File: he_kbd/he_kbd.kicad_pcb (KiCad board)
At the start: 2 copper layers, 162.2 x 126.5 mm, 165 parts, among them U1 CD74HC4067M, U2 CD74HC4067M, U3 CD74HC4067M

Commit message: continue
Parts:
- U1, U2, U3: footprint Package_SO:SOIC-24W_7.5x15.4mm_P1.27mm -> Package_SO:SSOP-24_3.9x8.7mm_P0.635mm
- moved U3 2.47 mm to (78.8, 54.2)
- moved U1 2.37 mm to (101.4, 115.9)
- moved U2 2.19 mm to (81.2, 93.4)
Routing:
- net Net-(HE_9-OUT): track 59.5 -> 125.4 mm, vias 2 -> 1
- net Net-(HE_10-OUT): track 44.2 -> 30.3 mm, vias 2 -> 1
- net Net-(HE_3-OUT): track 27.9 -> 20.4 mm
- net Net-(HE_8-OUT): track 75.3 -> 79.4 mm
- net Net-(HE_11-OUT): track 27.4 -> 31.6 mm
- net /MTP_EN_0: track 3.88 -> 0.00 mm, vias 1 -> 0
- net /MTP_BIN_2: track 3.42 -> 0.00 mm, vias 1 -> 0
- net Net-(HE_2-OUT): track 46.5 -> 43.4 mm
- net Net-(HE_1-OUT): track 62.6 -> 65.7 mm
- net Net-(HE_6-OUT): track 62.3 -> 59.2 mm
- net /MTP_BIN_3: track 2.21 -> 0.00 mm, vias 1 -> 0
- net Net-(HE_16-OUT): track 1.84 -> 0.00 mm, vias 1 -> 0
- net Net-(HE_15-OUT): track 1.83 -> 0.00 mm, vias 1 -> 0
- net Net-(HE_14-OUT): track 1.82 -> 0.00 mm, vias 1 -> 0
- net Net-(HE_13-OUT): track 1.81 -> 0.00 mm, vias 1 -> 0
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
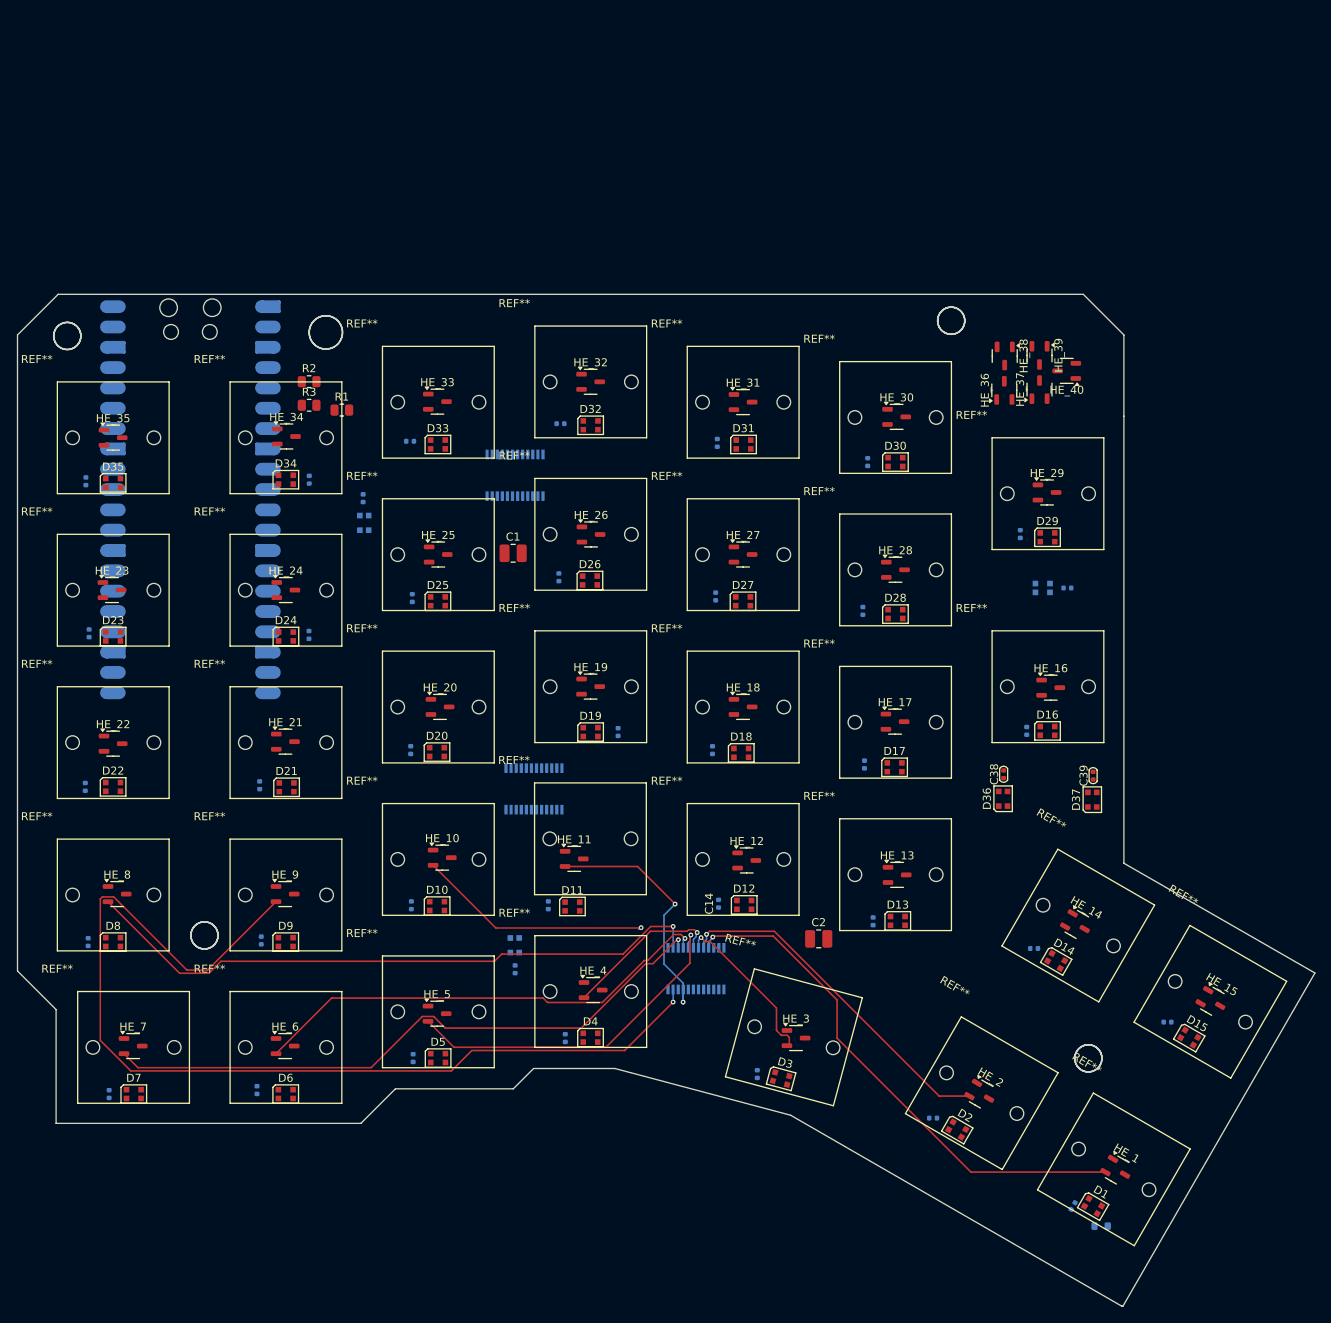
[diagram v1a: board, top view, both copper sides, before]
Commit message: fixed up the net classes
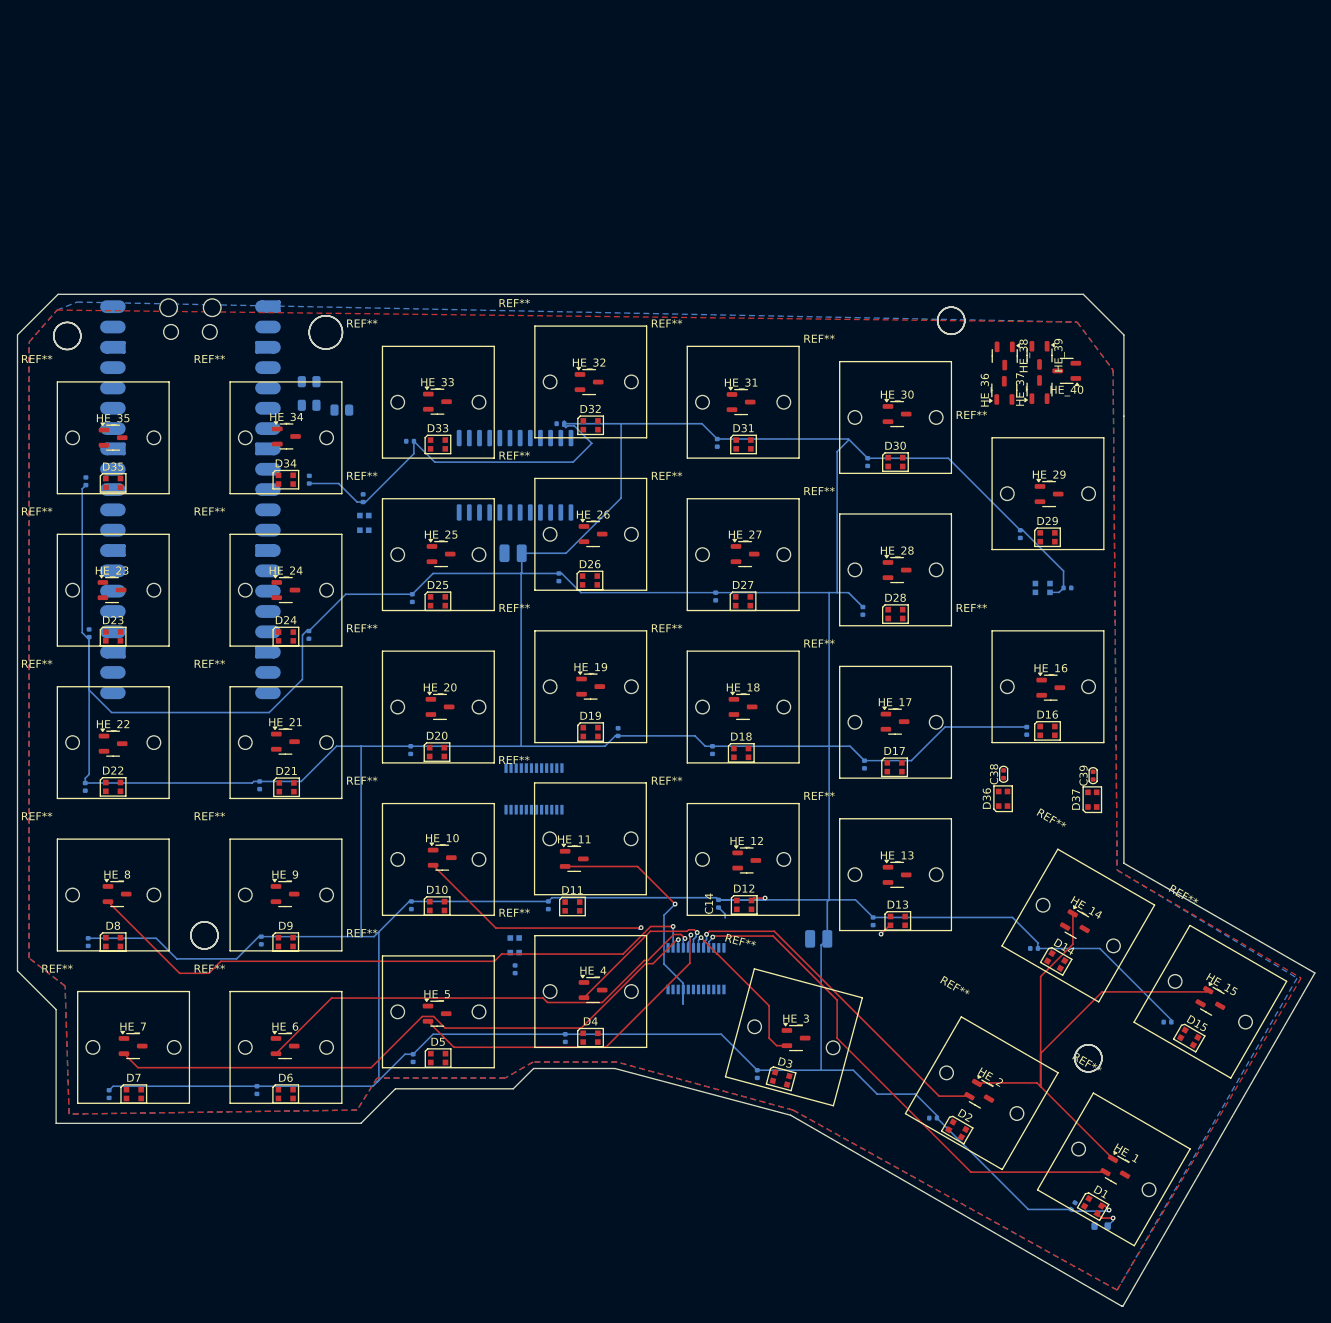
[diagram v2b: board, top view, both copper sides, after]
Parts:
- C1, C2, R1, R2, R3: moved to B.Cu
- U3: footprint Package_SO:SSOP-24_3.9x8.7mm_P0.635mm -> Package_SO:SOIC-24W_7.5x15.4mm_P1.27mm
- moved HE_32 28.6 mm to (88.1, 42.6)
- moved HE_25 28.5 mm to (69.6, 64.1)
- moved HE_30 26.1 mm to (126.6, 46.6)
- moved HE_27 25.5 mm to (107.6, 64.1)
- moved HE_31 25.0 mm to (107.1, 45.1)
- moved HE_26 25.0 mm to (88.6, 61.6)
- moved HE_29 21.4 mm to (145.6, 56.6)
- moved HE_28 21.1 mm to (126.6, 66.1)
- turned C1 to 180 degrees
- turned C2 to 180 degrees
- turned R1 to 180 degrees
- turned R2 to 180 degrees
- turned R3 to 180 degrees
- renumbered HE_32 to HE_25, HE_31 to HE_26, HE_30 to HE_27, HE_29 to HE_28, HE_28 to HE_29, HE_27 to HE_30, HE_26 to HE_31, HE_25 to HE_32
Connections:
- net Net-(HE_1-OUT) renamed /hesig1
- net Net-(HE_10-OUT) renamed /hesig10
- net Net-(HE_11-OUT) renamed /hesig11
- net Net-(HE_12-OUT) renamed /hesig12
- net Net-(HE_13-OUT) renamed /hesig13
- net Net-(HE_14-OUT) renamed /hesig14
- net Net-(HE_15-OUT) renamed /hesig15
- net Net-(HE_16-OUT) renamed /hesig16
- net Net-(HE_17-OUT) renamed /hesig17
- net Net-(HE_18-OUT) renamed /hesig18
- net Net-(HE_19-OUT) renamed /hesig19
- net Net-(HE_2-OUT) renamed /hesig2
- net Net-(HE_20-OUT) renamed /hesig20
- net Net-(HE_21-OUT) renamed /hesig21
- net Net-(HE_22-OUT) renamed /hesig22
- net Net-(HE_23-OUT) renamed /hesig23
- net Net-(HE_24-OUT) renamed /hesig24
- net Net-(HE_25-OUT) renamed /hesig32
- net Net-(HE_26-OUT) renamed /hesig31
- net Net-(HE_27-OUT) renamed /hesig30
- net Net-(HE_28-OUT) renamed /hesig29
- net Net-(HE_29-OUT) renamed /hesig28
- net Net-(HE_3-OUT) renamed /hesig3
- net Net-(HE_30-OUT) renamed /hesig27
- net Net-(HE_31-OUT) renamed /hesig26
- net Net-(HE_32-OUT) renamed /hesig25
- net Net-(HE_33-OUT) renamed /hesig33
- net Net-(HE_34-OUT) renamed /hesig34
- net Net-(HE_35-OUT) renamed /hesig35
- net Net-(HE_36-OUT) renamed /hesig36
- net Net-(HE_37-OUT) renamed /hesig37
- net Net-(HE_38-OUT) renamed /hesig38
- net Net-(HE_39-OUT) renamed /hesig39
- net Net-(HE_4-OUT) renamed /hesig4
- net Net-(HE_40-OUT) renamed /hesig40
- net Net-(HE_5-OUT) renamed /hesig5
- net Net-(HE_6-OUT) renamed /hesig6
- net Net-(HE_7-OUT) renamed /hesig7
- net Net-(HE_8-OUT) renamed /hesig8
- net Net-(HE_9-OUT) renamed /hesig9
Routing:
- net NEOPIXEL_POWER: track 0.00 -> 864.2 mm, vias 0 -> 2
- net /hesig9: track 125.4 -> 0.00 mm, vias 1 -> 0
- net /ANALOGUE_VIN: track 0.00 -> 72.6 mm
- net Net-(D1-DIN): track 0.00 -> 3.50 mm, vias 0 -> 1
- net GND: track 0.00 -> 3.29 mm, vias 0 -> 1
- net /hesig11: vias 2 -> 1
- added copper zone on F.Cu, net /ANALOGUE_GND
- added copper zone on B.Cu, net GND

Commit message: continue
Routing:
- net /ANALOGUE_VIN: track 72.6 -> 966.8 mm, vias 0 -> 4
- net NEOPIXEL_DATA: track 0.00 -> 199.1 mm, vias 0 -> 2
- net NEOPIXEL_POWER: track 864.2 -> 1016.8 mm, vias 2 -> 20
- net /hesig8: track 79.4 -> 0.00 mm, vias 1 -> 0
- net Net-(D15-DOUT): track 0.00 -> 48.5 mm, vias 0 -> 2
- net GND: track 3.29 -> 51.4 mm, vias 1 -> 20
- net Net-(D8-DOUT): track 0.00 -> 34.7 mm
- net /hesig11: track 31.6 -> 0.00 mm, vias 1 -> 0
- net /hesig10: track 30.3 -> 0.00 mm, vias 1 -> 0
- net Net-(D13-DOUT): track 0.00 -> 28.3 mm, vias 0 -> 2
- net Net-(D12-DOUT): track 0.00 -> 27.3 mm, vias 0 -> 2
- net Net-(D11-DOUT): track 0.00 -> 26.9 mm
- net Net-(D14-DOUT): track 0.00 -> 23.7 mm
- net Net-(D10-DIN): track 0.00 -> 23.3 mm
- net Net-(D3-DOUT): track 0.00 -> 22.5 mm
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
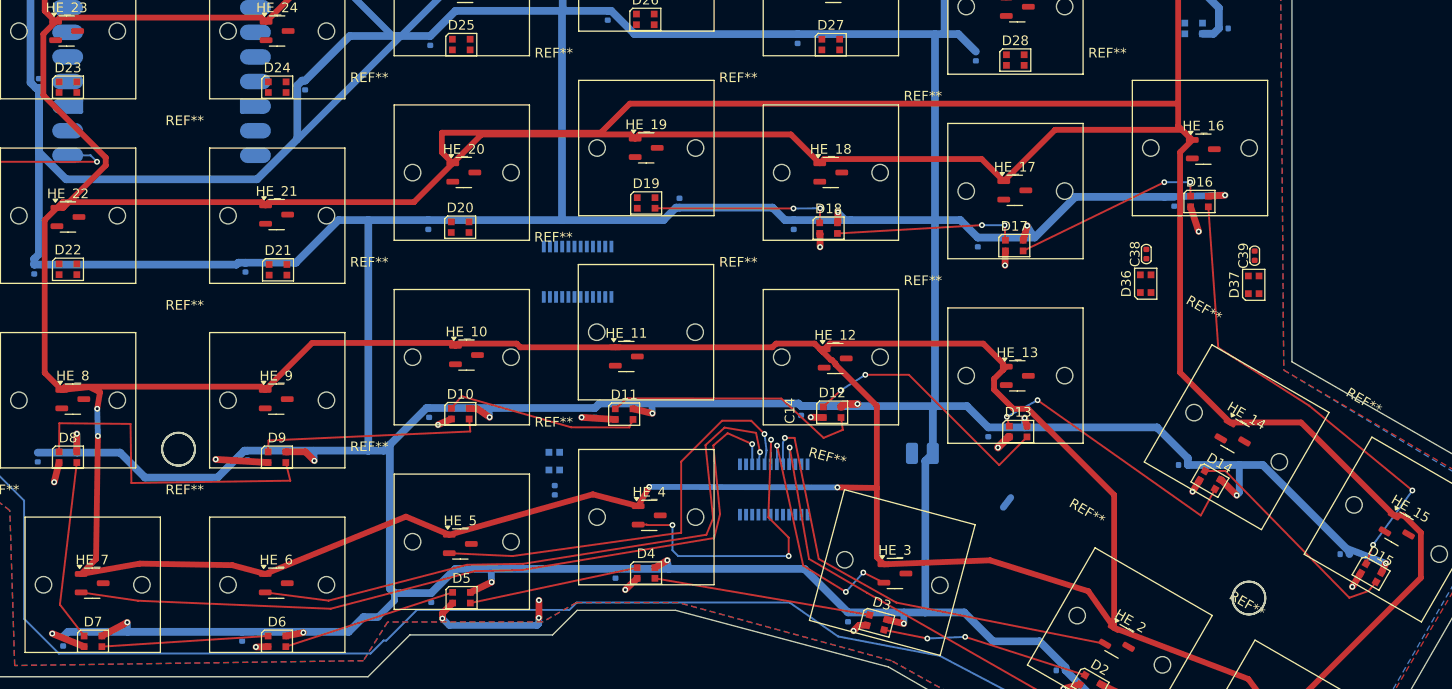
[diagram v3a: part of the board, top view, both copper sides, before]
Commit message: before updating pcb files, i added / changed some schematic components
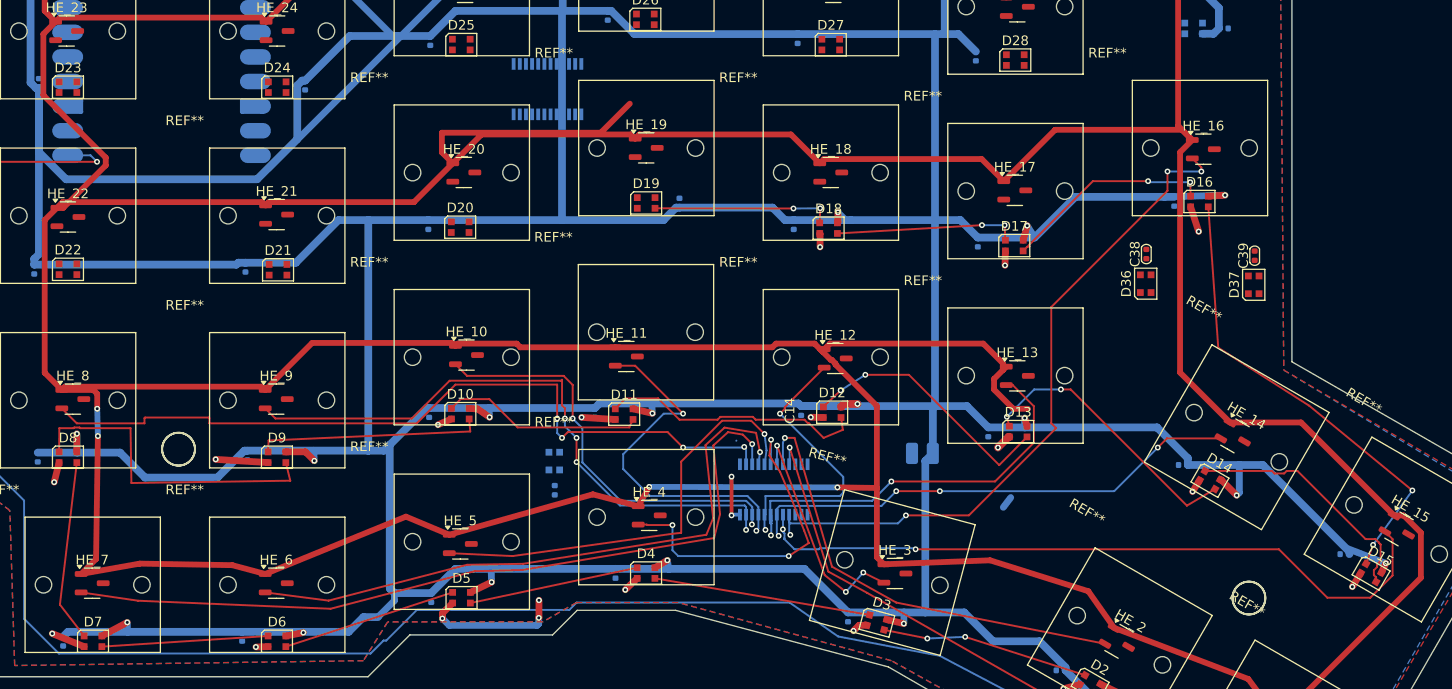
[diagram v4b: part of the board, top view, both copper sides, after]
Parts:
- moved U2 19.1 mm to (78.1, 74.6)
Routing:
- net /hesig8: track 0.00 -> 81.9 mm, vias 0 -> 4
- net /ANALOGUE_VIN: track 966.8 -> 889.4 mm, vias 4 -> 6
- net /hesig15: track 0.00 -> 73.8 mm, vias 0 -> 2
- net /hesig16: track 0.00 -> 71.5 mm, vias 0 -> 4
- net /hesig9: track 0.00 -> 63.7 mm, vias 0 -> 4
- net /hesig14: track 0.00 -> 51.7 mm, vias 0 -> 4
- net /hesig13: track 0.00 -> 42.8 mm, vias 0 -> 2
- net /hesig10: track 0.00 -> 42.7 mm, vias 0 -> 2
- net /hesig11: track 0.00 -> 36.6 mm, vias 0 -> 2
- net /hesig12: track 0.00 -> 29.3 mm, vias 0 -> 2
- net Net-(D14-DOUT): track 23.7 -> 25.7 mm
- net Net-(D16-DOUT): track 20.3 -> 21.8 mm
- net /hesig4: track 33.8 -> 35.0 mm
- net Net-(D8-DOUT): track 34.7 -> 33.8 mm
- net /hesig3: track 24.8 -> 24.0 mm
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
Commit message: much more organised now
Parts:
- removed R1, R2, R3: 10k, Resistor_SMD:R_0805_2012Metric
- removed REF** (x35): SW_Cherry_MX_1.00u_ANALOGUE, he_kbd_footprint:SW_Cherry_MX_1.00u_ANALOGUE
- added C43: 50u, Inductor_SMD:L_0603_1608Metric, B.Cu at (19.6, 59.7)
- added C44: 50u, Inductor_SMD:L_0603_1608Metric, B.Cu at (23.4, 98.2)
- added C45: 50u, Inductor_SMD:L_0603_1608Metric, B.Cu at (142.7, 41.3)
- added C46: 50u, Inductor_SMD:L_0603_1608Metric, B.Cu at (135.7, 49.6)
- added C47: 50u, Inductor_SMD:L_0603_1608Metric, B.Cu at (116.9, 64.6)
- added C48: 50u, Inductor_SMD:L_0603_1608Metric, B.Cu at (136.2, 80.0)
- added C49: 50u, Inductor_SMD:L_0603_1608Metric, B.Cu at (153.9, 110.7)
- added C50: 50u, Inductor_SMD:L_0603_1608Metric, B.Cu at (145.6, 135.4)
- added R5: 4.7k, Resistor_SMD:R_0402_1005Metric, B.Cu at (25.1, 66.1)
- added R6: 4.7k, Resistor_SMD:R_0402_1005Metric, B.Cu at (25.2, 65.0)
- added R7: 10k, Resistor_SMD:R_0603_1608Metric_Pad0.98x0.95mm_HandSolder, B.Cu at (71.8, 54.7)
- added R8: 10k, Resistor_SMD:R_0603_1608Metric_Pad0.98x0.95mm_HandSolder, B.Cu at (79.3, 81.4)
- added R9: 10k, Resistor_SMD:R_0603_1608Metric_Pad0.98x0.95mm_HandSolder, B.Cu at (96.0, 120.8)
- added SW1: ~, he_kbd_footprint:SW_Cherry_MX_1.00u_ANALOGUE, F.Cu at (151.1, 131.4)
- added SW10: ~, he_kbd_footprint:SW_Cherry_MX_1.00u_ANALOGUE, F.Cu at (62.2, 95.2)
- added SW11: ~, he_kbd_footprint:SW_Cherry_MX_1.00u_ANALOGUE, F.Cu at (81.3, 92.7)
- added SW12: ~, he_kbd_footprint:SW_Cherry_MX_1.00u_ANALOGUE, F.Cu at (100.3, 95.4)
- added SW13: ~, he_kbd_footprint:SW_Cherry_MX_1.00u_ANALOGUE, F.Cu at (119.3, 97.1)
- added SW14: ~, he_kbd_footprint:SW_Cherry_MX_1.00u_ANALOGUE, F.Cu at (146.7, 100.9)
- added SW15: ~, he_kbd_footprint:SW_Cherry_MX_1.00u_ANALOGUE, F.Cu at (163.2, 110.4)
- added SW16: ~, he_kbd_footprint:SW_Cherry_MX_1.00u_ANALOGUE, F.Cu at (138.4, 73.6)
- added SW17: ~, he_kbd_footprint:SW_Cherry_MX_1.00u_ANALOGUE, F.Cu at (119.4, 78.1)
- added SW18: ~, he_kbd_footprint:SW_Cherry_MX_1.00u_ANALOGUE, F.Cu at (100.3, 76.2)
- added SW19: ~, he_kbd_footprint:SW_Cherry_MX_1.00u_ANALOGUE, F.Cu at (81.2, 73.6)
- added SW2: ~, he_kbd_footprint:SW_Cherry_MX_1.00u_ANALOGUE, F.Cu at (134.6, 121.9)
- added SW20: ~, he_kbd_footprint:SW_Cherry_MX_1.00u_ANALOGUE, F.Cu at (62.2, 76.2)
- added SW21: ~, he_kbd_footprint:SW_Cherry_MX_1.00u_ANALOGUE, F.Cu at (43.2, 80.6)
- added SW22: ~, he_kbd_footprint:SW_Cherry_MX_1.00u_ANALOGUE, F.Cu at (21.6, 80.6)
- added SW23: ~, he_kbd_footprint:SW_Cherry_MX_1.00u_ANALOGUE, F.Cu at (21.6, 61.5)
- added SW24: ~, he_kbd_footprint:SW_Cherry_MX_1.00u_ANALOGUE, F.Cu at (43.2, 61.5)
- added SW25: ~, he_kbd_footprint:SW_Cherry_MX_1.00u_ANALOGUE, F.Cu at (62.2, 57.1)
- added SW26: ~, he_kbd_footprint:SW_Cherry_MX_1.00u_ANALOGUE, F.Cu at (81.3, 54.6)
- added SW27: ~, he_kbd_footprint:SW_Cherry_MX_1.00u_ANALOGUE, F.Cu at (100.3, 57.1)
- added SW28: ~, he_kbd_footprint:SW_Cherry_MX_1.00u_ANALOGUE, F.Cu at (119.3, 59.0)
- added SW29: ~, he_kbd_footprint:SW_Cherry_MX_1.00u_ANALOGUE, F.Cu at (138.4, 49.5)
- added SW3: ~, he_kbd_footprint:SW_Cherry_MX_1.00u_ANALOGUE, F.Cu at (108.7, 115.9)
- added SW30: ~, he_kbd_footprint:SW_Cherry_MX_1.00u_ANALOGUE, F.Cu at (119.3, 40.0)
- added SW31: ~, he_kbd_footprint:SW_Cherry_MX_1.00u_ANALOGUE, F.Cu at (100.3, 38.1)
- added SW32: ~, he_kbd_footprint:SW_Cherry_MX_1.00u_ANALOGUE, F.Cu at (81.3, 35.5)
- added SW33: ~, he_kbd_footprint:SW_Cherry_MX_1.00u_ANALOGUE, F.Cu at (62.2, 38.0)
- added SW34: ~, he_kbd_footprint:SW_Cherry_MX_1.00u_ANALOGUE, F.Cu at (43.2, 42.5)
- added SW35: ~, he_kbd_footprint:SW_Cherry_MX_1.00u_ANALOGUE, F.Cu at (21.6, 42.5)
- added SW4: ~, he_kbd_footprint:SW_Cherry_MX_1.00u_ANALOGUE, F.Cu at (81.3, 111.7)
- added SW5: ~, he_kbd_footprint:SW_Cherry_MX_1.00u_ANALOGUE, F.Cu at (62.2, 114.3)
- added SW6: ~, he_kbd_footprint:SW_Cherry_MX_1.00u_ANALOGUE, F.Cu at (43.2, 118.7)
- added SW7: ~, he_kbd_footprint:SW_Cherry_MX_1.00u_ANALOGUE, F.Cu at (24.1, 118.7)
- added SW8: ~, he_kbd_footprint:SW_Cherry_MX_1.00u_ANALOGUE, F.Cu at (21.6, 99.7)
- added SW9: ~, he_kbd_footprint:SW_Cherry_MX_1.00u_ANALOGUE, F.Cu at (43.2, 99.6)
- AM0: renamed from U1; footprint Package_SO:SSOP-24_3.9x8.7mm_P0.635mm -> Package_SO:SSOP-24_5.3x8.2mm_P0.65mm
- AM1: renamed from U2; footprint Package_SO:SSOP-24_3.9x8.7mm_P0.635mm -> Package_SO:SSOP-24_5.3x8.2mm_P0.65mm
- AM2: renamed from U3; footprint Package_SO:SOIC-24W_7.5x15.4mm_P1.27mm -> Package_SO:SSOP-24_5.3x8.2mm_P0.65mm
- C1: value 500u -> 50u
- C10, C11, C12, C13, C14, C15, C16, C17, C18, C19, C20, C21, C22, C23, C24, C25, C26, C27, C28, C29, C3, C30, C31, C32, C33, C34, C35, C36, C37, C38, C39, C4, C40, C41, C42, C5, C6, C7, C8, C9: value 1u -> 100n
- moved C2 37.7 mm to (153.7, 119.6)
- moved C1 18.4 mm to (96.8, 66.2)
- moved AM1 1.87 mm to (76.7, 73.4), turned to 180 degrees
- moved AM0 1.29 mm to (102.7, 115.8), turned to 180 degrees
- moved D37 0.54 mm to (150.5, 94.6)
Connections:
- A1 pad 26: unconnected-(A1-GPIO20-Pad26) -> I2C0_SDA
- A1 pad 27: unconnected-(A1-GPIO21-Pad27) -> I2C0_SCL
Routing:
- net NEOPIXEL_POWER: track 1016.8 -> 841.9 mm
- net /ANALOGUE_VIN: track 889.4 -> 797.6 mm, vias 6 -> 11
- net /hesig7: track 82.9 -> 0.00 mm, vias 1 -> 0
- net /hesig8: track 81.9 -> 0.00 mm, vias 4 -> 0
- net /hesig15: track 73.8 -> 0.00 mm, vias 2 -> 0
- net /hesig16: track 71.5 -> 0.00 mm, vias 4 -> 0
- net /hesig1: track 65.0 -> 0.00 mm, vias 1 -> 0
- net /hesig6: track 65.0 -> 0.00 mm, vias 1 -> 0
- net /hesig9: track 63.7 -> 0.00 mm, vias 4 -> 0
- net /hesig14: track 51.7 -> 0.00 mm, vias 4 -> 0
- net /hesig2: track 47.2 -> 0.00 mm, vias 1 -> 0
- net /hesig5: track 45.5 -> 0.00 mm, vias 1 -> 0
- net /hesig13: track 42.8 -> 0.00 mm, vias 2 -> 0
- net /hesig10: track 42.7 -> 0.00 mm, vias 2 -> 0
- net /hesig11: track 36.6 -> 0.00 mm, vias 2 -> 0
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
